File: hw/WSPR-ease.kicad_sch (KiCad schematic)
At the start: 42 parts, among them J101 GNSS Ant, J102 Tx Ant, J103 pwr+data, Q101 MMBF170, U101 ATGM336H-5N31, U102 ESP32-S3-WROOM-1-N8R8, U103 TPS22918DBVR, U104 TPS74612PQWDRBRQ1, U105 SRV05-4, U106 LMR51430

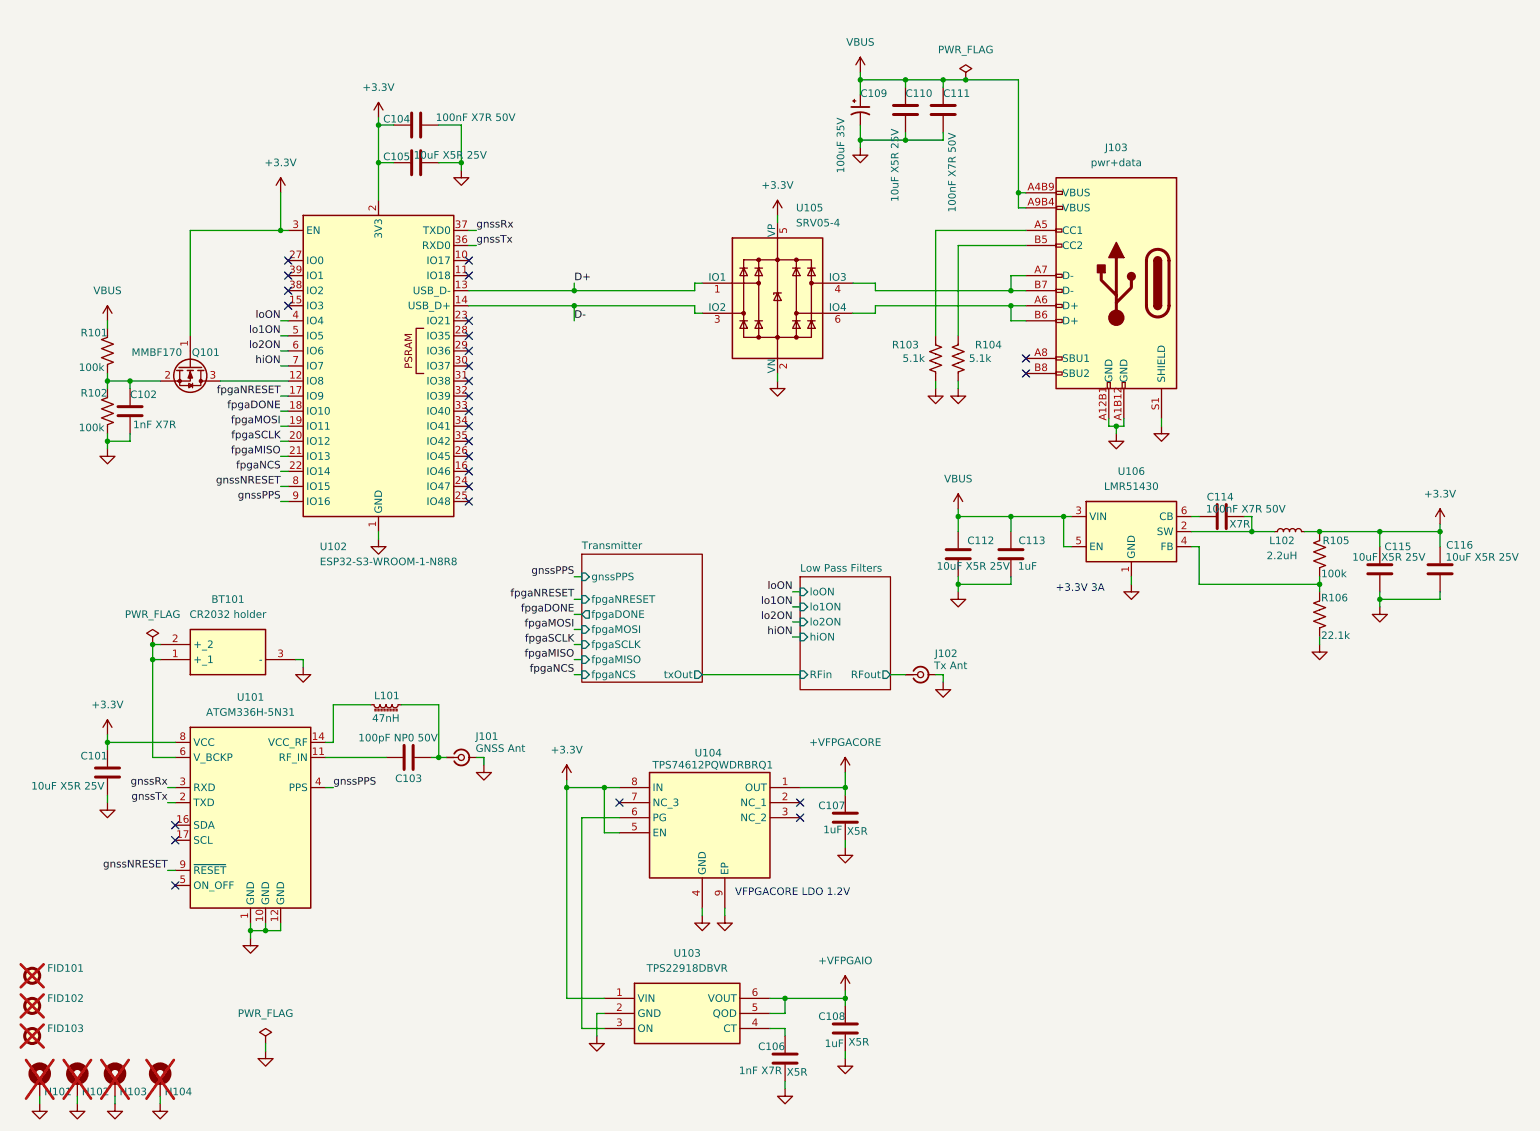
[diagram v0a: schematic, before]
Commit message: Cleanup and prep for MacroFab quote
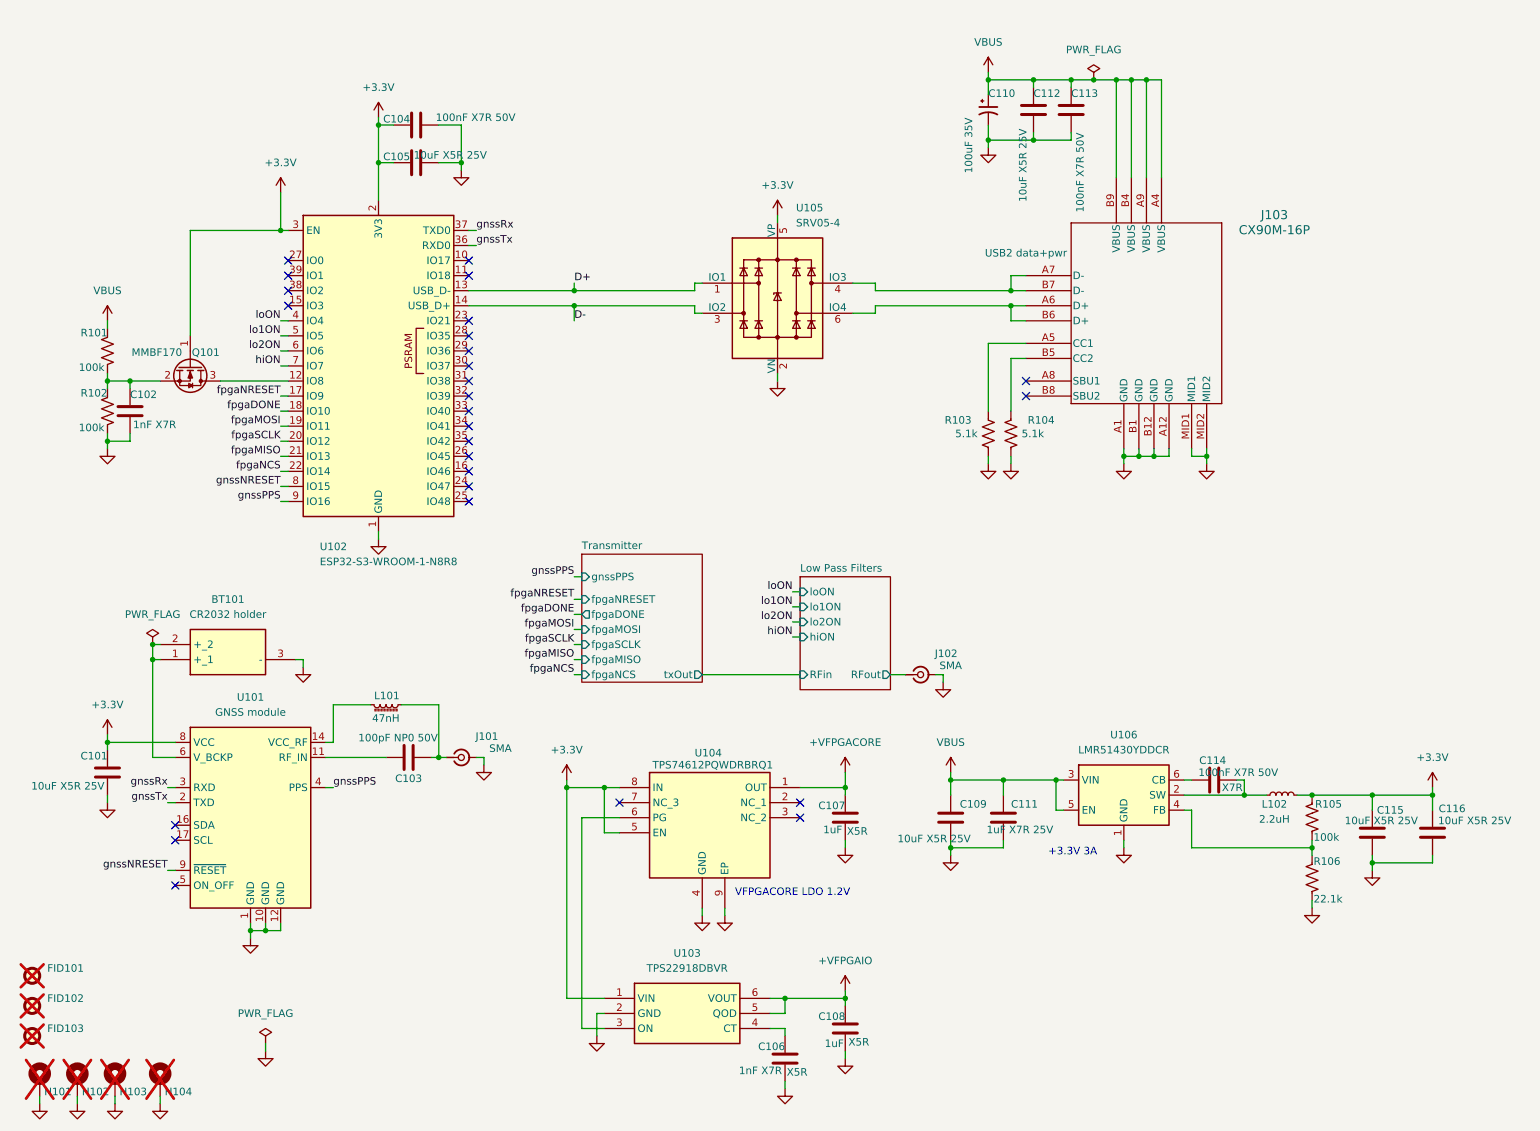
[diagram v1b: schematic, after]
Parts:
- removed J103: pwr+data, Library:USB_C_Receptacle_HRO_TYPE-C-31-M-12-bursted, symbol Library:USB_C_Receptacle_USB2.0_16P-bursted
- added J103: CX90M-16P, CX90M-16P_HIR, symbol Library:CX90M-16P
- C110: renamed from C109; footprint Library:CAPAE850X1050N -> Capacitor_SMD:C_Elec_6.3x7.7
- C111: renamed from C113; value 1uF -> 1uF X7R 25V; footprint Capacitor_SMD:C_0402_1005Metric -> Capacitor_SMD:C_0603_1608Metric
- J101: value GNSS Ant -> SMA; footprint Connector_Coaxial:SMA_BAT_Wireless_BWSMA-KWE-Z001 -> Library:SMA_Amphenol_901-143_Horizontal; label (none) -> GNSS Ant
- J102: value Tx Ant -> SMA; footprint Connector_Coaxial:SMA_BAT_Wireless_BWSMA-KWE-Z001 -> Library:SMA_Amphenol_901-143_Horizontal; label (none) -> TX Ant
- U101: value ATGM336H-5N31 -> GNSS module; MPN ATGM336H-5N31 -> Teseo-LIV3R
- U106: value LMR51430 -> LMR51430YDDCR
- renumbered C112 to C109, C110 to C112, C111 to C113
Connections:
- net GND: now also J103.A1 (GND), J103.A12 (GND), J103.B1 (GND), J103.B12 (GND), J103.MID1, J103.MID2
- net VBUS: now also J103.A4 (VBUS), J103.A9 (VBUS), J103.B4 (VBUS), J103.B9 (VBUS)
- net at U105.4 (IO3): now also J103.A7 (D-), J103.B7 (D-)
- net at U105.6 (IO4): now also J103.A6 (D+), J103.B6 (D+)
- net at R103.1: now also J103.A5 (CC1)
- net at R104.1: now also J103.B5 (CC2)
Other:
- moved on the sheet: C109, C110, C111, C112, C113, C114, C115, C116, L102, R103, R104, R105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

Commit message: Parts ordered for DVT1 build
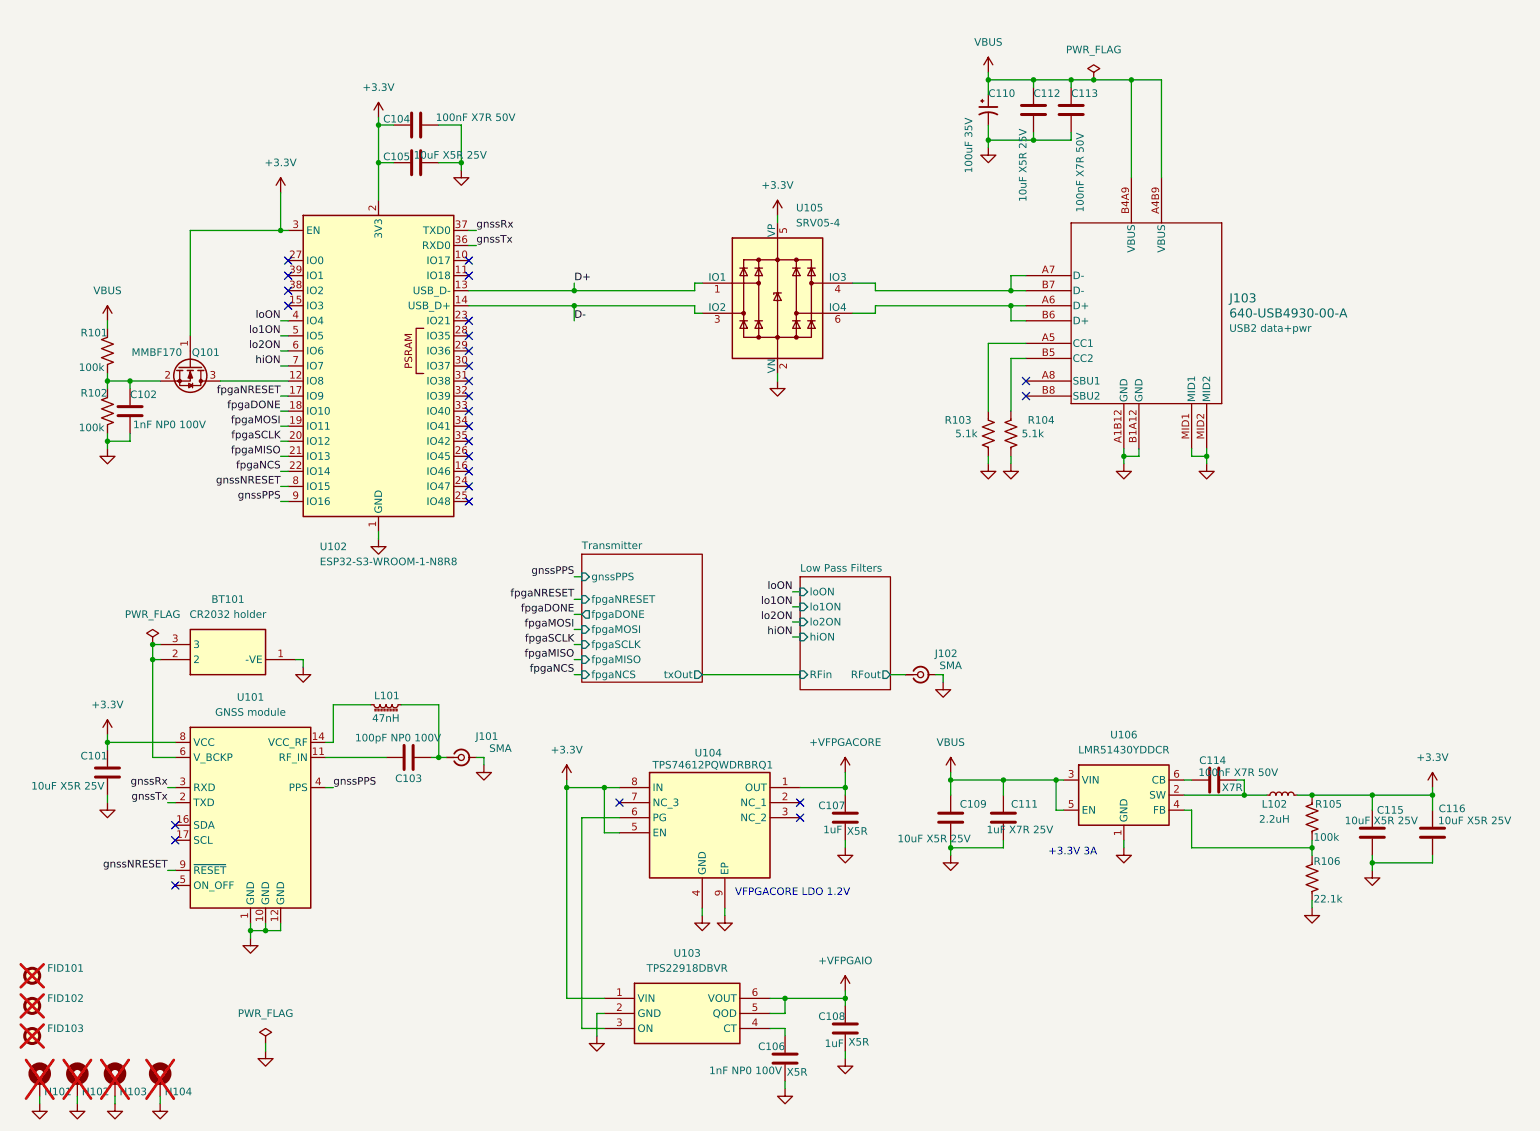
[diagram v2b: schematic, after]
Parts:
- BT101: footprint BATHLD014THM -> Library:S8401-46; symbol Library:BAT-HLD-014-THM -> Library:S8401-46; MFG (none) -> Harwin; MPN (none) -> S8401-46; Manufacturer_Name TE Connectivity -> Harwin; Manufacturer_Part_Number BAT-HLD-014-THM -> S8401-46; Mouser Part Number 712-BAT-HLD-014-THM -> 855-S8401-46; Mouser Price/Stock https://www.mouser.co.uk/ProductDetail/Linx-Technologies/BA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 -> https://www.mouser.co.uk/ProductDetail/Harwin/S8401-46?qs=Q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; Mouser_PN (none) -> 855-S8401-46
- C101, C105, C112, C115, C116: MFG (none) -> Kyocera AVX; MPN (none) -> CM105X5R106M25AT; Mouser_PN (none) -> 346-CM105X5R106M25AT
- C102: value 1nF X7R -> 1nF NP0 100V; footprint Capacitor_SMD:C_0402_1005Metric -> Capacitor_SMD:C_0603_1608Metric; LCSC C106205 -> C5182455; MFG (none) -> Kyocera AVX; MPN (none) -> KGM15ACG2A102FT; Mouser_PN (none) -> 581-KGM15ACG2A102FT
- C103: value 100pF NP0 50V -> 100pF NP0 100V; footprint Capacitor_SMD:C_0402_1005Metric -> Capacitor_SMD:C_0603_1608Metric; MFG (none) -> Kyocera AVX; MPN (none) -> KGM15ACG2A101FT; Mouser_PN (none) -> 581-KGM15ACG2A101FT
- C104, C113: MFG (none) -> Kyocera AVX; MPN (none) -> KGM15BR71H104KT; Mouser_PN (none) -> 581-KGM15BR71H104KT
- C106: value 1nF X7R -> 1nF NP0 100V; footprint Capacitor_SMD:C_0402_1005Metric -> Capacitor_SMD:C_0603_1608Metric; LCSC C106205 -> C5182455; MFG (none) -> Kyocera AVX; MPN (none) -> KGM15ACG2A102FT; Mouser_PN 81-GRM155R61E105KE1D -> 581-KGM15ACG2A102FT
- C107, C108: MFG (none) -> muRata; MPN (none) -> GRM155Z71A105KE1D; Mouser_PN 81-GRM155R61E105KE1D -> 81-GRM155Z71A105KE1D
- C109: MFG (none) -> Kyocera AVX; MPN (none) -> CM105X5R106M25AT; Mouser_PN 963-MLAST168BB5106MT -> 346-CM105X5R106M25AT
- C110: footprint Capacitor_SMD:C_Elec_6.3x7.7 -> Capacitor_SMD:C_Elec_8x6.2; MFG (none) -> Vishay; MPN (none) -> MAL214297007E3; Mouser_PN (none) -> 71-MAL214297007E3
- C111: MFG (none) -> Kyocera AVX; MPN (none) -> CM105X7R105K25AT; Mouser_PN 81-GRM155R61E105KE1D -> 346-CM105X7R105K25AT
- C114: MFG (none) -> Kyocera AVX; MPN (none) -> KGM15BR71H104KT; Mouser_PN 80-C0805F104K1RAUTO -> 581-KGM15BR71H104KT
- J101, J102: MFG (none) -> Samtec; MPN (none) -> SMA-J-P-H-RA-TH1; Mouser_PN (none) -> 200-SMAJPHRATH1
- J103: value CX90M-16P -> 640-USB4930-00-A; footprint CX90M-16P_HIR -> Library:USB_C_Receptacle_HRO_TYPE-C-31-M-12-bursted; symbol Library:CX90M-16P -> Library:USB2-C-16pin; MFG (none) -> GCT; MPN (none) -> USB4930-00-A; Mouser_PN (none) -> 640-USB4930-00-A
- L101: MFG (none) -> Abracon; MPN (none) -> AIMC-0603-47NJ-T; Mouser_PN (none) -> 815-AIMC-0603-47NJT
- L102: footprint Inductor_SMD:L_0805_2012Metric -> Inductor_SMD:L_1008_2520Metric; MFG (none) -> Abracon; MPN (none) -> AIML-1008HC-2R2M-T; Mouser_PN (none) -> 815-AIML-1008HC2R2MT
- Q101: MFG (none) -> Diodes inc; MPN (none) -> MMBF170Q-13-F; Mouser_PN (none) -> 621-MMBF170Q-13-F
- R101, R102, R105: MFG (none) -> Bourns; MPN (none) -> CRT0402-FZ-1003GLF; Mouser_PN (none) -> 652-CRT0402FZ1003GLF
- R103, R104: MFG (none) -> Vishay; MPN (none) -> MCS04020C5101FE000; Mouser_PN (none) -> 594-MCS04020C5101FE0
- R106: MFG (none) -> Yageo; MPN (none) -> RT0402FRD0722K1L; Mouser_PN (none) -> 603-RT0402FRD0722K1L
- U101: MFG (none) -> STMicro; MPN Teseo-LIV3R -> TESEO-LIV3R; Mouser_PN (none) -> 511-TESEO-LIV3R
- U102: MFG (none) -> Espressif; MPN (none) -> ESP32-S3-WROOM-1-N8R8; Mouser_PN (none) -> 356-EP32S3WROOM1N8R8
- U103: MFG (none) -> TI
- U104: footprint SON65P300X300X100-9N-D -> Library:SON65P300X300X100-9N-D; MFG (none) -> TI
- U105: MFG (none) -> Semtech; MPN (none) -> SRV05-4.TCT; Mouser_PN (none) -> 947-SRV05-4.TCT
- U106: MFG (none) -> TI; MPN (none) -> LMR51430YDDCR; Mouser_PN (none) -> 595-LMR51430YDDCR
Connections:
- net GND: now also BT101.1 (-VE), J103.A1B12 (GND), J103.B1A12 (GND); no longer BT101.3 (-), J103.A1 (GND), J103.A12 (GND), J103.B1 (GND), J103.B12 (GND)
- net VBUS: now also J103.A4B9 (VBUS), J103.B4A9 (VBUS); no longer J103.A4 (VBUS), J103.A9 (VBUS), J103.B4 (VBUS), J103.B9 (VBUS)
- net at BT101.2, U101.6 (V_BCKP): now also BT101.3; no longer BT101.1 (+_1)

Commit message: About to redo the layout of the tx gate controls to match lengths
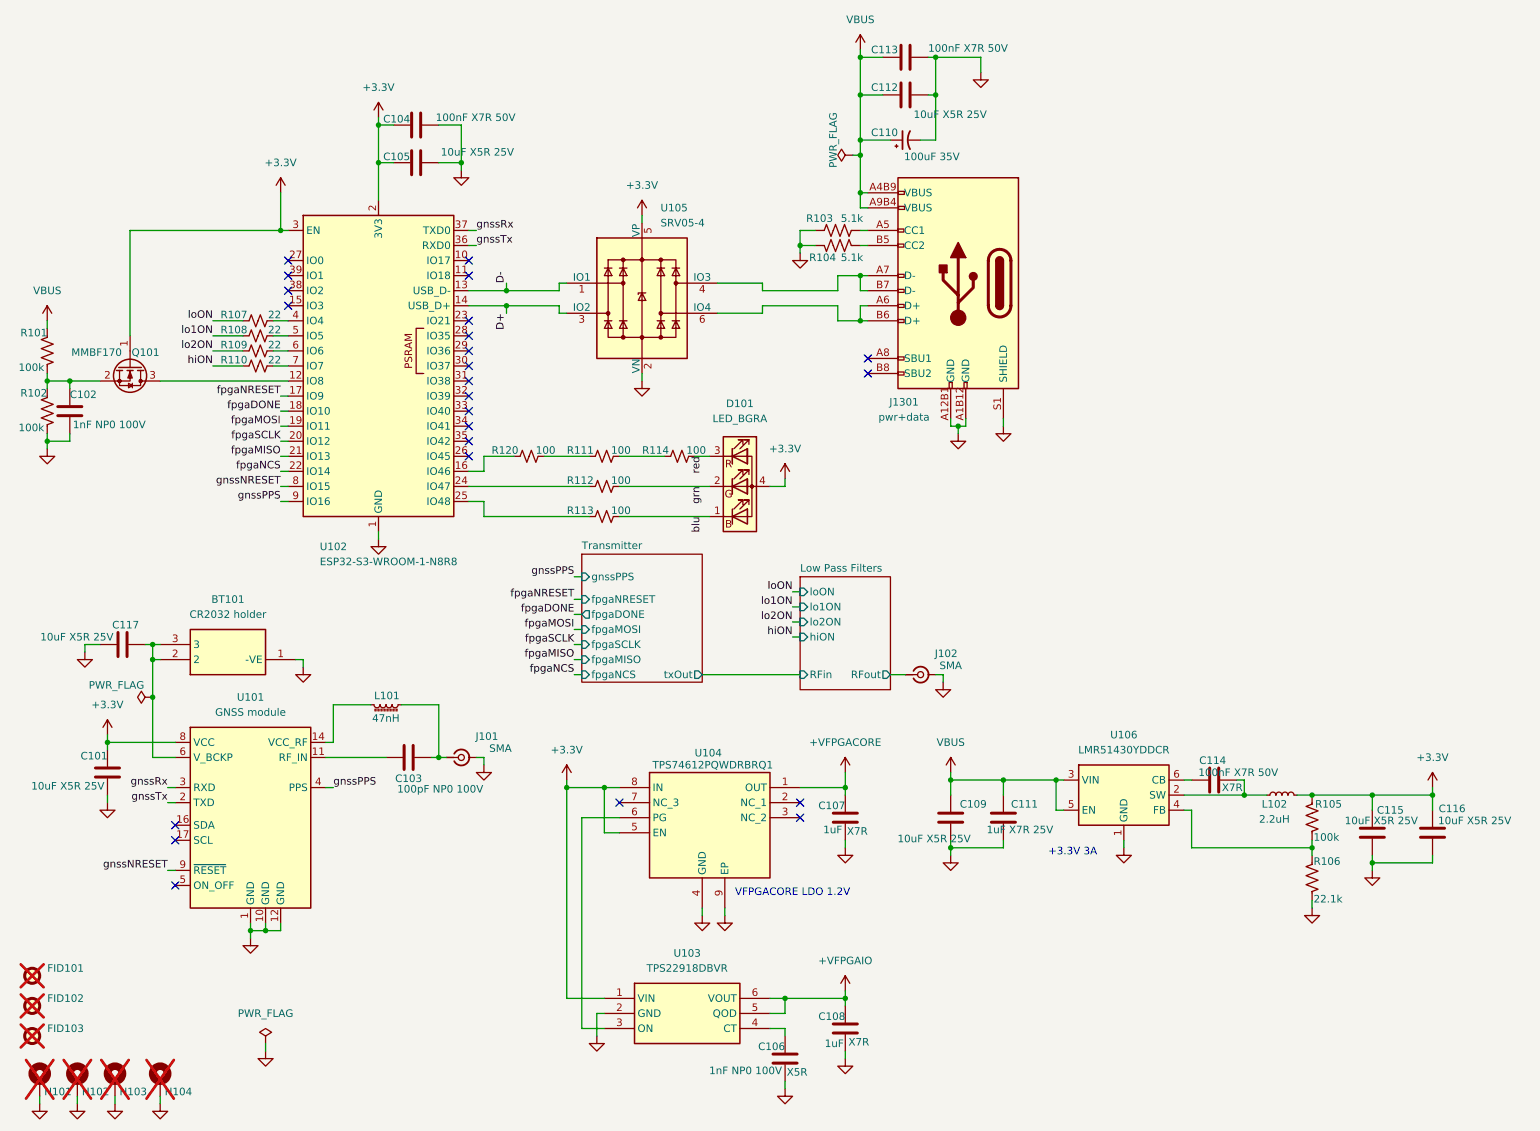
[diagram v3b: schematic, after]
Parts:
- removed J103: 640-USB4930-00-A, Library:USB_C_Receptacle_HRO_TYPE-C-31-M-12-bursted, symbol Library:USB2-C-16pin
- added C117: 10uF X5R 25V, Capacitor_SMD:C_0603_1608Metric, symbol Device:C
- added D101: LED_BGRA, Library:UHD111AFKAC3K23E1L3VG5ZB3Z3, symbol Device:LED_BGRA
- added J1301: pwr+data, Library:USB_C_Receptacle_HRO_TYPE-C-31-M-12-bursted, symbol Library:USB_C_Receptacle_USB2.0_16P-bursted
- added R107, R108, R109, R110: 22, Resistor_SMD:R_0402_1005Metric, symbol Device:R_Small_US
- added R111, R112, R113, R114, R120: 100, Resistor_SMD:R_0402_1005Metric, symbol Device:R_Small_US
- C107, C108: cap-type X5R -> X7R; working-voltage 25V -> 10V
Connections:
- net +3.3V: now also D101.4 (A)
- net D+: now also U102.14 (USB_D+), U105.3 (IO2); no longer U102.13 (USB_D-), U105.1 (IO1)
- net D-: now also U102.13 (USB_D-), U105.1 (IO1); no longer U102.14 (USB_D+), U105.3 (IO2)
- net GND: now also C117.1, J1301.A12B1 (GND), J1301.A1B12 (GND), J1301.S1 (SHIELD)
- net VBUS: now also J1301.A4B9 (VBUS), J1301.A9B4 (VBUS)
- net hiON: now also R110.1; no longer U102.7 (IO7)
- net lo1ON: now also R108.1; no longer U102.5 (IO5)
- net lo2ON: now also R109.1; no longer U102.6 (IO6)
- net loON: now also R107.1; no longer U102.4 (IO4)
- net at BT101.2, BT101.3, U101.6 (V_BCKP): now also C117.2
- net at U105.4 (IO3): now also J1301.A7 (D-), J1301.B7 (D-)
- net at U105.6 (IO4): now also J1301.A6 (D+), J1301.B6 (D+)
- net at R103.1: now also J1301.A5 (CC1)
- net at U102.16 (IO46): now also R120.1
- net at U102.24 (IO47): now also R112.1
- net at U102.25 (IO48): now also R113.1
- net at R104.1: now also J1301.B5 (CC2)
- new net: R111.1, R120.2
- new net: R108.2, U102.5 (IO5)
- new net: R111.2, R114.1
- new net: R107.2, U102.4 (IO4)
- new net: R110.2, U102.7 (IO7)
- new net: R109.2, U102.6 (IO6)
- new net blu: D101.1 (BK), R113.2
- new net grn: D101.2 (GK), R112.2
- new net red: D101.3 (RK), R114.2
- no-connect marks 27 -> 24
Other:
- moved on the sheet: C102, C110, C112, C113, Q101, R101, R102, R103, R104, U105
